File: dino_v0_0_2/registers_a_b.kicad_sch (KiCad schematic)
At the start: 10 parts, among them U31 74LS373, U32 74LS373, U41 74LS245, U42 74LS245, U54 74LS04, U55 74LS02, U56 74LS121, U59 74LS00

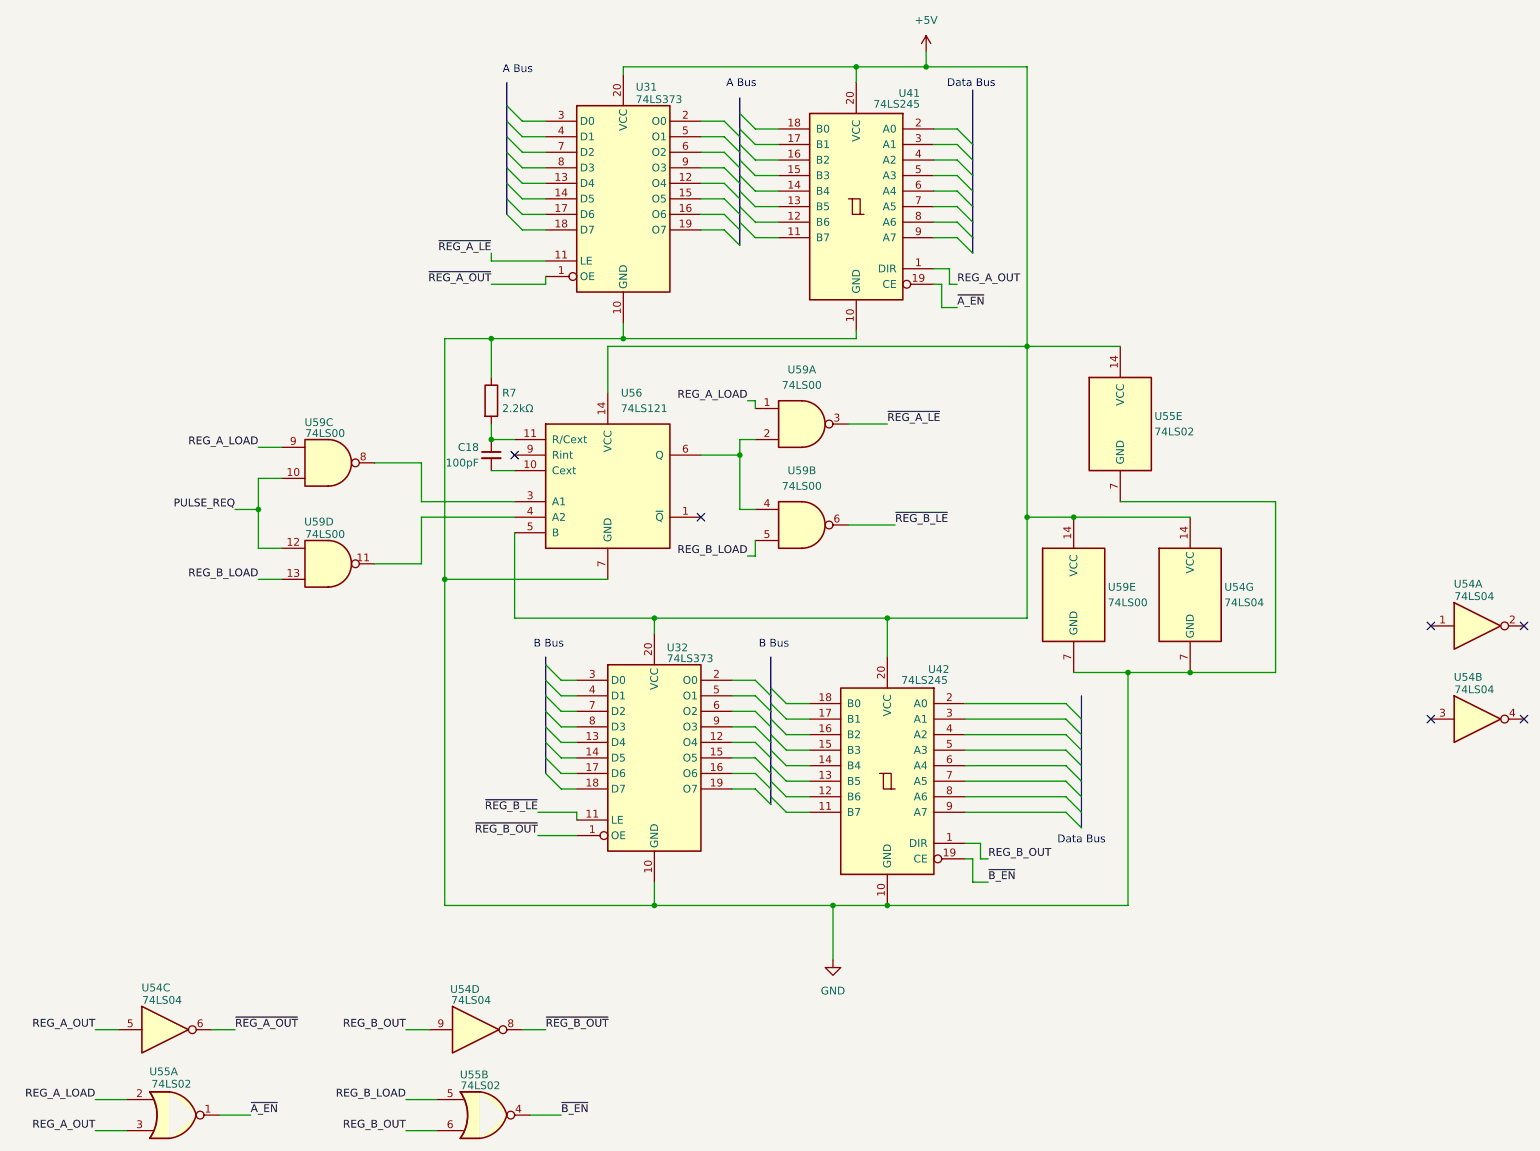
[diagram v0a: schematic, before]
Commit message: KiCAD Update
- Fixed Pins to match hardware
- Fixed DIR on '245 Pair for Reg A+B
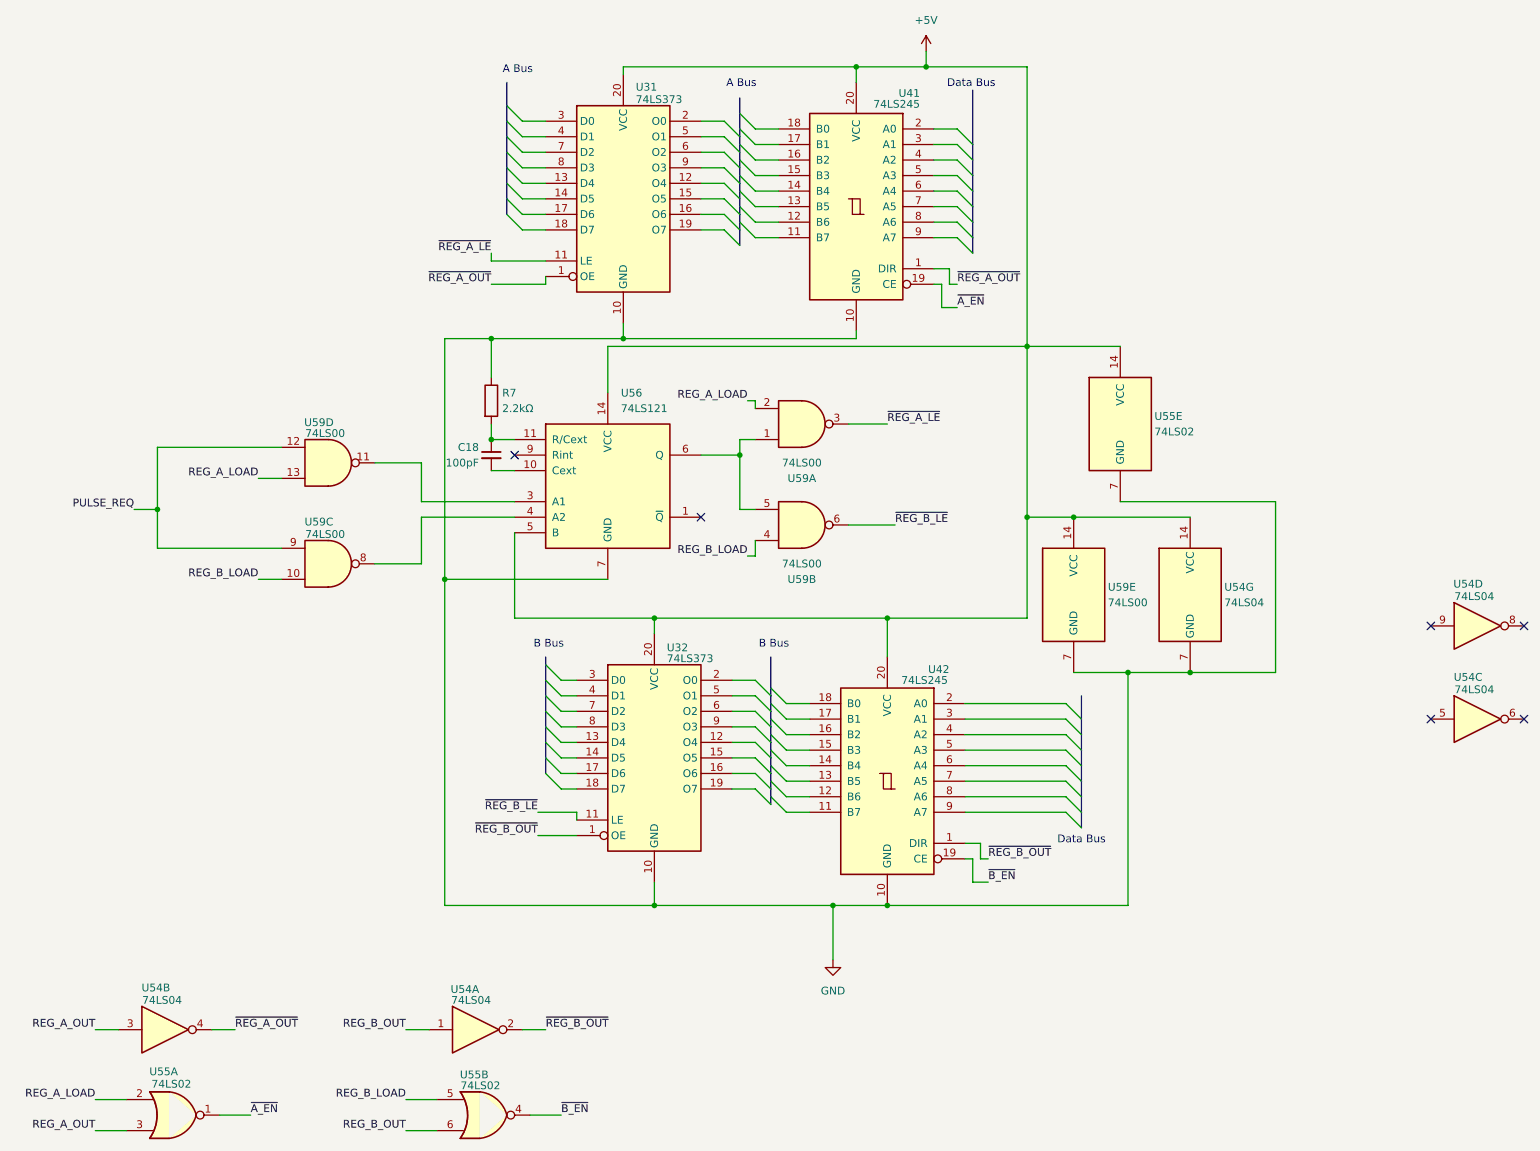
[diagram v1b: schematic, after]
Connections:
- net PULSE_REQ: now also U59.12, U59.9; no longer U59.10, U59.12
- net REG_A_LOAD: now also U59.13, U59.2; no longer U59.1, U59.9
- net REG_A_OUT: now also U54.3; no longer U41.1 (DIR), U54.5
- net REG_B_LOAD: now also U59.10, U59.4; no longer U59.13, U59.5
- net REG_B_OUT: now also U54.1; no longer U42.1 (DIR), U54.9
- net ~{REG_A_OUT}: now also U41.1 (DIR), U54.4; no longer U54.6
- net ~{REG_B_OUT}: now also U42.1 (DIR), U54.2; no longer U54.8
- net at U56.4 (A2): now also U59.8; no longer U59.11
- net at U56.3 (A1): now also U59.11; no longer U59.8
- new net: U56.6 (Q), U59.1, U59.5
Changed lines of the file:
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@@
 	)
 	(junction
-		(at 55.88 96.52)
+		(at 39.37 96.52)
 		(diameter 0)
 		(color 0 0 0 0)
@@
 	(wire
 		(pts
-			(xy 52.07 96.52) (xy 55.88 96.52)
+			(xy 35.56 96.52) (xy 39.37 96.52)
 		)
 		(stroke
@@
 	(wire
 		(pts
-			(xy 55.88 86.36) (xy 59.69 86.36)
+			(xy 55.88 91.44) (xy 59.69 91.44)
 		)
 		(stroke
@@
 	(wire
 		(pts
+			(xy 59.69 102.87) (xy 39.37 102.87)
+		)
+		(stroke
+			(width 0)
+			(type default)
+		)
+	)
+	(wire
+		(pts
 			(xy 128.27 87.63) (xy 134.62 87.63)
 		)
@@
 	(wire
 		(pts
+			(xy 39.37 96.52) (xy 39.37 102.87)
+		)
+		(stroke
+			(width 0)
+			(type default)
+		)
+	)
+	(wire
+		(pts
 			(xy 172.72 157.48) (xy 172.72 153.67)
 		)
@@
 	(wire
 		(pts
-			(xy 55.88 91.44) (xy 59.69 91.44)
-		)
-		(stroke
-			(width 0)
-			(type default)
-		)
-	)
-	(wire
-		(pts
 			(xy 171.45 130.81) (xy 187.96 130.81)
 		)
@@
 	(wire
 		(pts
-			(xy 55.88 107.95) (xy 59.69 107.95)
-		)
-		(stroke
-			(width 0)
-			(type default)
-		)
-	)
-	(wire
-		(pts
 			(xy 170.18 63.5) (xy 167.64 63.5)
 		)
@@
 	(wire
 		(pts
-			(xy 55.88 96.52) (xy 55.88 91.44)
-		)
-		(stroke
-			(width 0)
-			(type default)
-		)
-	)
-	(wire
-		(pts
 			(xy 142.24 140.97) (xy 146.05 140.97)
 		)
@@
 	(wire
 		(pts
-			(xy 142.24 146.05) (xy 146.05 146.05)
+			(xy 39.37 86.36) (xy 59.69 86.36)
 		)
 		(stroke
@@
 	(wire
 		(pts
-			(xy 128.27 50.8) (xy 132.08 50.8)
+			(xy 142.24 146.05) (xy 146.05 146.05)
 		)
 		(stroke
@@
 	(wire
 		(pts
-			(xy 55.88 96.52) (xy 55.88 102.87)
+			(xy 128.27 50.8) (xy 132.08 50.8)
 		)
 		(stroke
@@
 	(wire
 		(pts
-			(xy 55.88 102.87) (xy 59.69 102.87)
-		)
-		(stroke
-			(width 0)
-			(type default)
-		)
-	)
-	(wire
-		(pts
 			(xy 128.27 43.18) (xy 132.08 43.18)
 		)
@@
 		)
 	)
+	(wire
+		(pts
+			(xy 39.37 86.36) (xy 39.37 96.52)
+		)
+		(stroke
+			(width 0)
+			(type default)
+		)
+	)
 	(bus
 		(pts
@@
 	(wire
 		(pts
+			(xy 55.88 107.95) (xy 59.69 107.95)
+		)
+		(stroke
+			(width 0)
+			(type default)
+		)
+	)
+	(wire
+		(pts
 			(xy 181.61 24.13) (xy 181.61 69.85)
 		)
@@
 		)
 	)
-	(label "REG_B_OUT"
+	(label "~{REG_B_OUT}"
 		(at 175.26 153.67 0)
 		(effects
@@
 		)
 	)
-	(label "REG_B_OUT"
-		(at 80.01 181.61 180)
+	(label "REG_B_LOAD"
+		(at 55.88 107.95 180)
 		(effects
 			(font
@@
 		)
 	)
-	(label "REG_B_LOAD"
-		(at 55.88 107.95 180)
+	(label "REG_B_OUT"
+		(at 80.01 181.61 180)
 		(effects
 			(font
@@
 		)
 	)
-	(label "REG_A_OUT"
+	(label "~{REG_A_OUT}"
 		(at 170.18 59.69 0)
 		(effects
@@
 	)
 	(label "PULSE_REQ"
-		(at 52.07 96.52 180)
+		(at 35.56 96.52 180)
 		(effects
 			(font
@@
 	)
 	(label "REG_A_LOAD"
-		(at 55.88 86.36 180)
+		(at 55.88 91.44 180)
 		(effects
 			(font
@@
 		(lib_id "74xx:74LS04")
 		(at 255.27 115.57 0)
-		(unit 1)
+		(unit 4)
 		(exclude_from_sim no)
 		(in_bom yes)
@@
 				(path "/e43166a5-d972-471d-b3cf-9f4f12c7f541/de772b95-eca4-4f61-9f12-d1e28130490b"
 					(reference "U54")
-					(unit 1)
+					(unit 4)
 				)
 			)
@@
 		(lib_id "74xx:74LS00")
 		(at 144.78 82.55 0)
+		(mirror x)
 		(unit 1)
 		(exclude_from_sim no)
@@
 		(on_board yes)
 		(dnp no)
-		(fields_autoplaced yes)
 		(property "Reference" "U59"
-			(at 144.7717 73.66 0)
+			(at 144.7717 91.44 0)
 			(effects
 				(font
@@
 		)
 		(property "Value" "74LS00"
-			(at 144.7717 76.2 0)
+			(at 144.7717 88.9 0)
 			(effects
 				(font
@@
 		(lib_id "74xx:74LS00")
 		(at 67.31 105.41 0)
-		(unit 4)
+		(unit 3)
 		(exclude_from_sim no)
 		(in_bom yes)
@@
 				(path "/e43166a5-d972-471d-b3cf-9f4f12c7f541/de772b95-eca4-4f61-9f12-d1e28130490b"
 					(reference "U59")
-					(unit 4)
+					(unit 3)
 				)
 			)
@@
 		(lib_id "74xx:74LS04")
 		(at 255.27 130.81 0)
-		(unit 2)
+		(unit 3)
 		(exclude_from_sim no)
 		(in_bom yes)
@@
 				(path "/e43166a5-d972-471d-b3cf-9f4f12c7f541/de772b95-eca4-4f61-9f12-d1e28130490b"
 					(reference "U54")
-					(unit 2)
+					(unit 3)
 				)
 			)
@@
 		(lib_id "74xx:74LS00")
 		(at 144.78 99.06 0)
+		(mirror x)
 		(unit 2)
 		(exclude_from_sim no)
@@
 		(on_board yes)
 		(dnp no)
-		(fields_autoplaced yes)
 		(property "Reference" "U59"
-			(at 144.7717 90.17 0)
+			(at 144.7717 107.95 0)
 			(effects
 				(font
@@
 		)
 		(property "Value" "74LS00"
-			(at 144.7717 92.71 0)
+			(at 144.7717 105.41 0)
 			(effects
 				(font
@@
 		(lib_id "74xx:74LS04")
 		(at 91.44 181.61 0)
-		(unit 4)
+		(unit 1)
 		(exclude_from_sim no)
 		(in_bom yes)
@@
 				(path "/e43166a5-d972-471d-b3cf-9f4f12c7f541/de772b95-eca4-4f61-9f12-d1e28130490b"
 					(reference "U54")
-					(unit 4)
+					(unit 1)
 				)
 			)
@@
 		(lib_id "74xx:74LS00")
 		(at 67.31 88.9 0)
-		(unit 3)
+		(unit 4)
 		(exclude_from_sim no)
 		(in_bom yes)
@@
 				(path "/e43166a5-d972-471d-b3cf-9f4f12c7f541/de772b95-eca4-4f61-9f12-d1e28130490b"
 					(reference "U59")
-					(unit 3)
+					(unit 4)
 				)
 			)
@@
 		(lib_id "74xx:74LS04")
 		(at 40.64 181.61 0)
-		(unit 3)
+		(unit 2)
 		(exclude_from_sim no)
 		(in_bom yes)
@@
 				(path "/e43166a5-d972-471d-b3cf-9f4f12c7f541/de772b95-eca4-4f61-9f12-d1e28130490b"
 					(reference "U54")
-					(unit 3)
+					(unit 2)
 				)
 			)

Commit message: Separate Registers from Trigger Logic
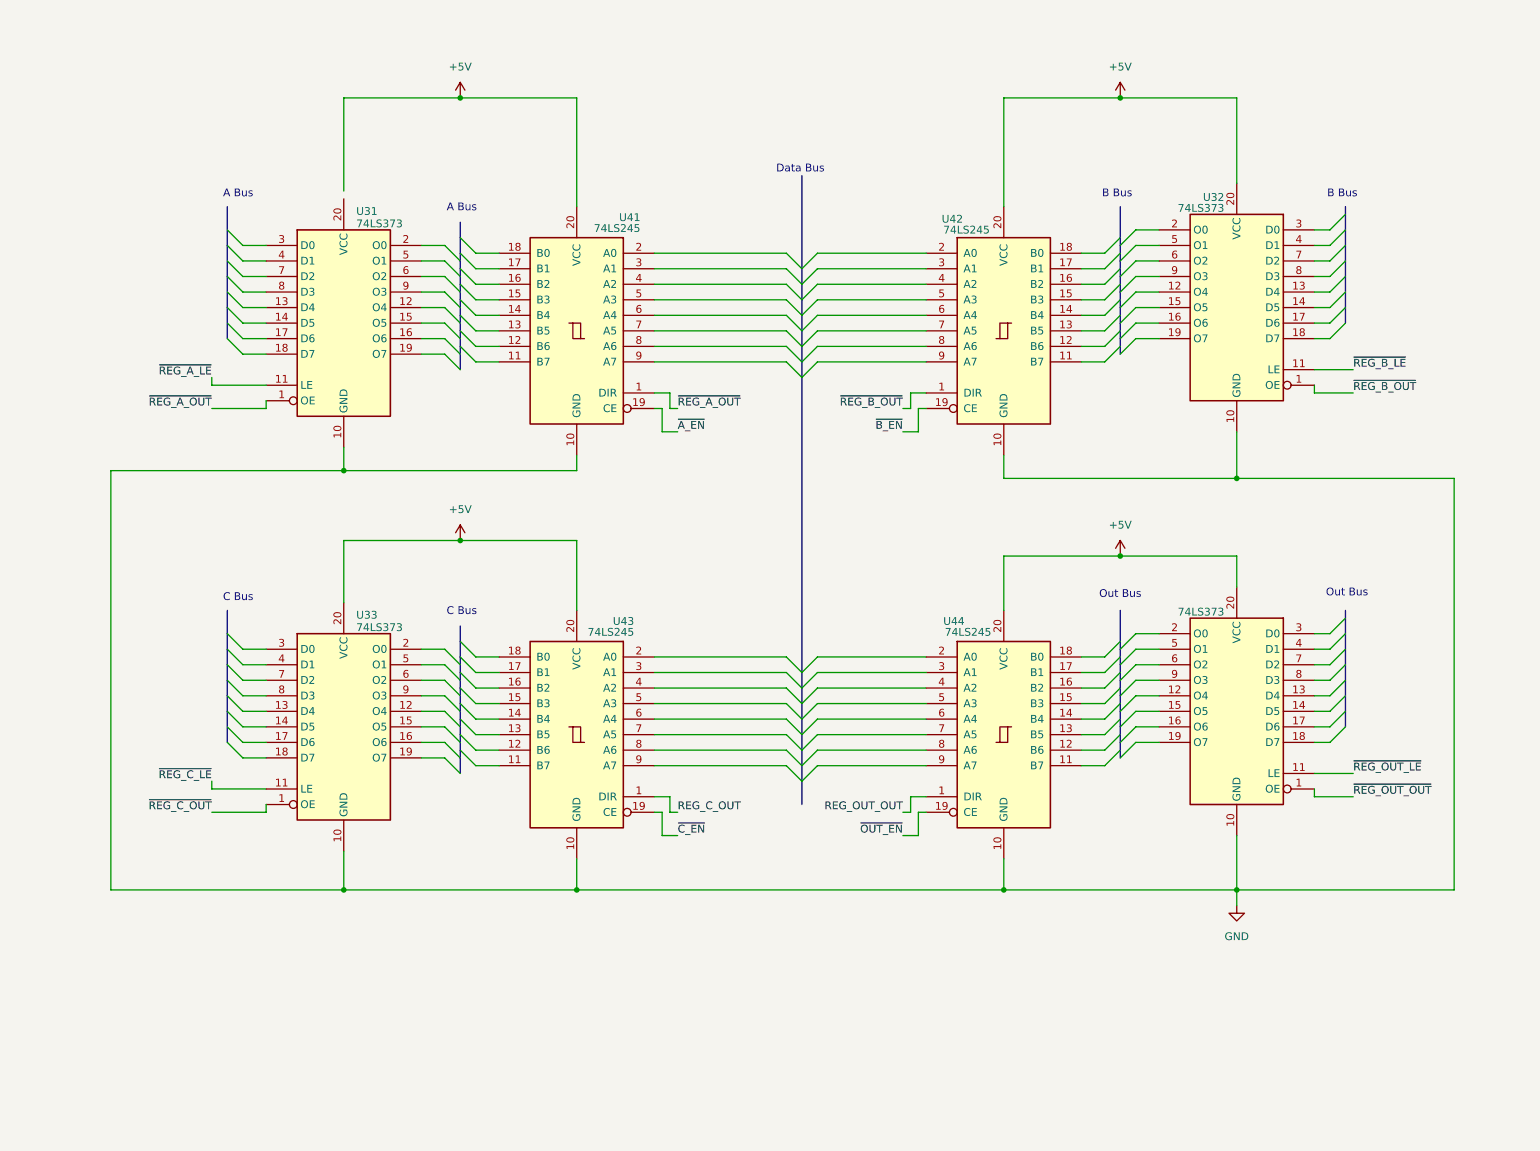
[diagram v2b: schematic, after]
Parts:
- removed C18: 100pF, symbol Device:C_Small
- removed R7: 2.2kΩ, symbol Device:R
- removed U54: 74LS04, symbol 74xx:74LS04
- removed U55: 74LS02, symbol 74xx:74LS02
- removed U56: 74LS121, symbol 74xx:74LS121
- removed U59: 74LS00, symbol 74xx:74LS00
- added U33, U35: 74LS373, symbol 74xx:74LS373
- added U43, U44: 74LS245, symbol 74xx:74LS245
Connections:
- net +5V: now also U33.20 (VCC), U35.20 (VCC), U43.20 (VCC), U44.20 (VCC); no longer U31.20 (VCC)
- net GND: now also U33.10 (GND), U35.10 (GND), U43.10 (GND), U44.10 (GND)
- new net REG_C_OUT: U43.1 (DIR)
- new net REG_OUT_OUT: U44.1 (DIR)
- new net ~{C_EN}: U43.19 (CE)
- new net ~{OUT_EN}: U44.19 (CE)
- new net ~{REG_C_LE}: U33.11 (LE)
- new net ~{REG_C_OUT}: U33.1 (OE)
- new net ~{REG_OUT_LE}: U35.11 (LE)
- new net ~{REG_OUT_OUT}: U35.1 (OE)
- no-connect marks 6 -> 0
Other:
- note added: "C Bus"
- note added: "Out Bus"
- moved on the sheet: U31, U32, U41, U42
